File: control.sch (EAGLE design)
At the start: 67 parts, among them IC3 ATTINY85-20S

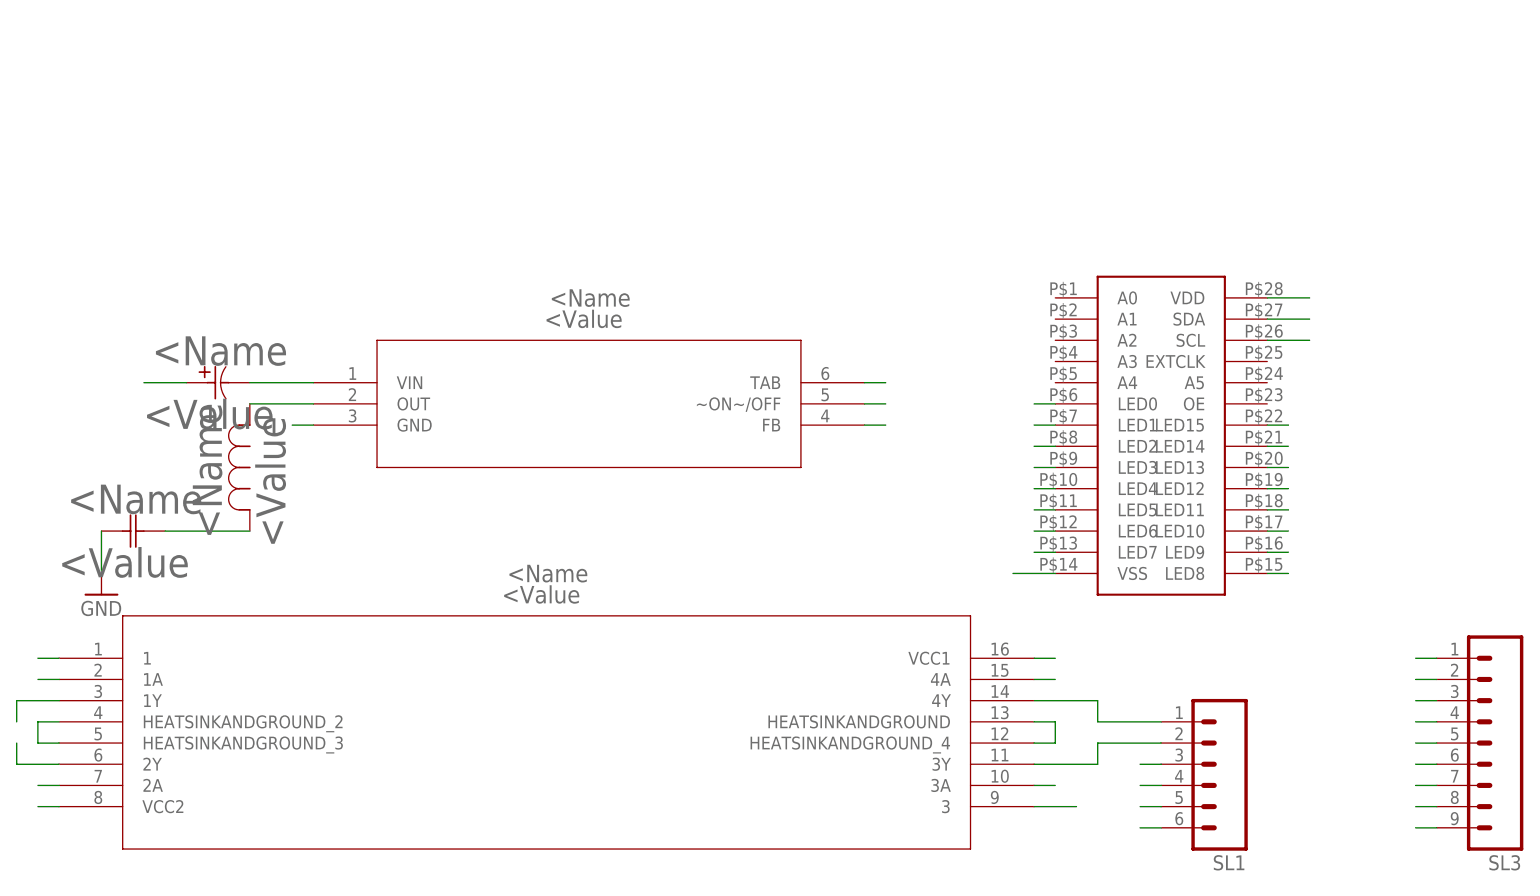
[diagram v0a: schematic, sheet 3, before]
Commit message: adds new components
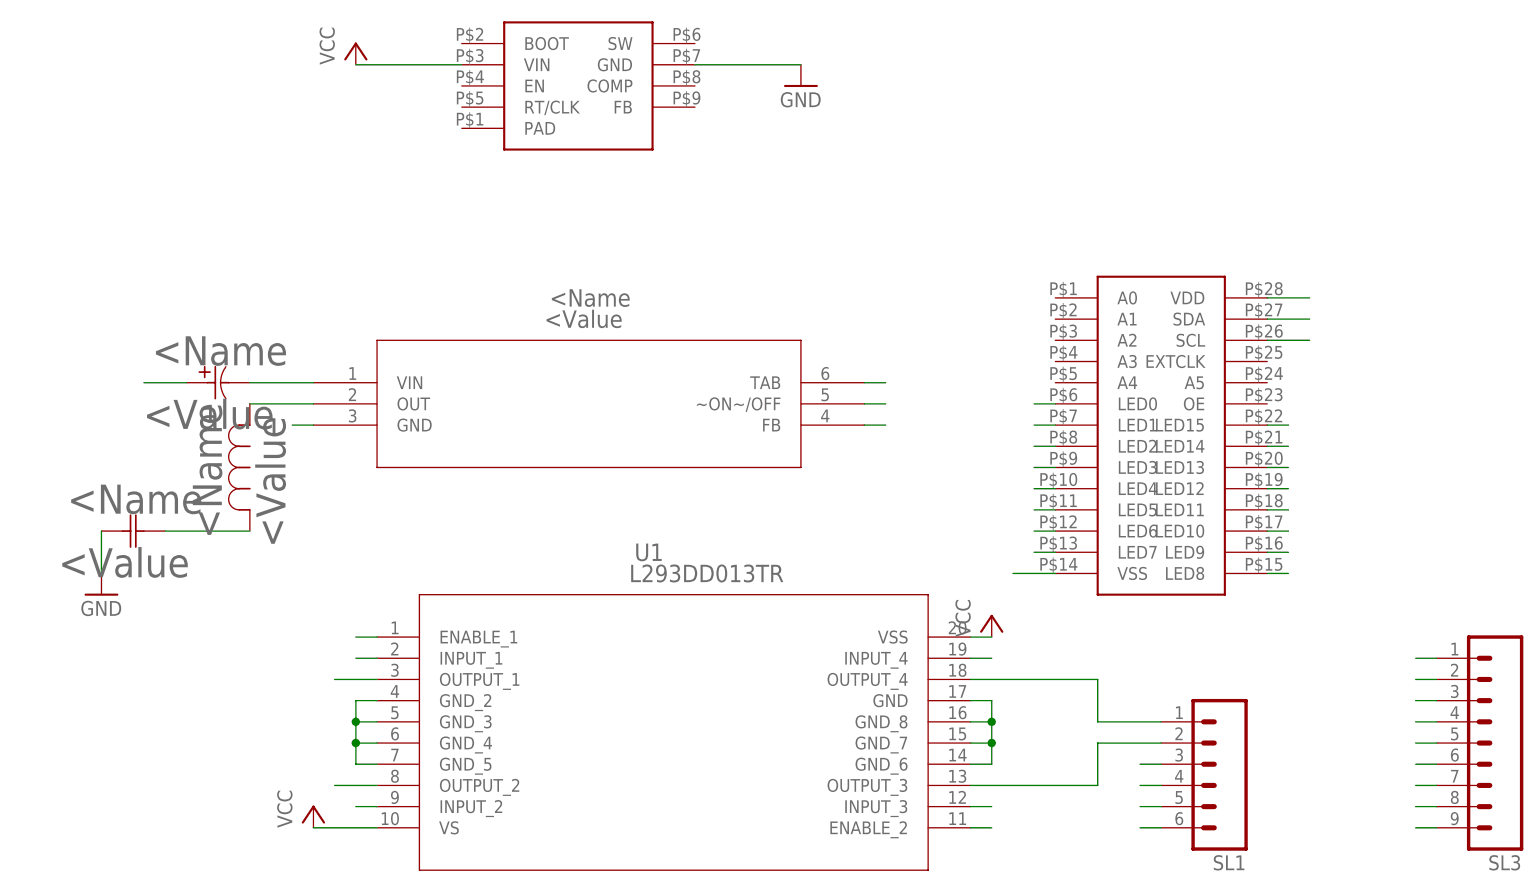
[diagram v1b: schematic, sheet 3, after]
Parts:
- removed U$2: L293DNE, LED Driver:L293DNE
- added U$35: NUD4011DR2G, Smile_Shade:NUD4011DR2G
- added U1: L293DD013TR, Smile_Shade:L293DD013TR
- U$11, U$13, U$15, U$17, U$19, U$21, U$23, U$25, U$27, U$29, U$3, U$31, U$33, U$40, U$5, U$7, U$9: device LED Driver:NUD4011DR2G -> Smile_Shade:NUD4011DR2G
- U$42: value NUD4011DR2G -> TPS54560DDAR; device LED Driver:NUD4011DR2G -> Smile_Shade:TPS54560DDAR
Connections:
- removed net M0: U$1.PWM0, U$2.1
- new net DIR1B: U1.INPUT_2
- new net DIR2A: U1.INPUT_4
- new net DIR2B: U1.INPUT_3
- new net M2: U$1.PWM1, U1.ENABLE_2
- new net N$42: U1.GND_2, U1.GND_3, U1.GND_4, U1.GND_5
- new net N$43: U1.GND, U1.GND_6, U1.GND_7, U1.GND_8
- new net VIN: SL3.1, U$1.CHG-IN, U$42.VIN
- net 3V3: no longer U$2.VCC1
- net 48: now also U$35.VIN; no longer U$40.VIN
- net 48V: now also U$40.VIN; no longer SL3.1, U$42.VIN
- net 5V: now also U1.VSS; no longer U$2.VCC2
- net DIR1A: now also U1.INPUT_1; no longer U$2.2A
- net GND: now also U$42.GND; no longer U$2.HEATSINKANDGROUND, U$2.HEATSINKANDGROUND_2, U$2.HEATSINKANDGROUND_3, U$2.HEATSINKANDGROUND_4
- net LEDSTR_10: now also U$23.LED1, U$23.LED2, U$23.LED3, U$23.LED4; no longer U$21.LED1, U$21.LED2, U$21.LED3, U$21.LED4
- net LEDSTR_11: now also U$21.LED1, U$21.LED2, U$21.LED3, U$21.LED4; no longer U$23.LED1, U$23.LED2, U$23.LED3, U$23.LED4
- net LEDSTR_12: now also U$19.LED1, U$19.LED2, U$19.LED3, U$19.LED4; no longer U$25.LED1, U$25.LED2, U$25.LED3, U$25.LED4
- net LEDSTR_17: now also U$35.LED1, U$35.LED2, U$35.LED3, U$35.LED4; no longer U$40.LED1, U$40.LED2, U$40.LED3, U$40.LED4
- net LEDSTR_18: now also U$40.LED1, U$40.LED2, U$40.LED3, U$40.LED4; no longer U$42.LED1, U$42.LED2, U$42.LED3, U$42.LED4
- net LEDSTR_9: now also U$25.LED1, U$25.LED2, U$25.LED3, U$25.LED4; no longer U$19.LED1, U$19.LED2, U$19.LED3, U$19.LED4
- net M1: now also U$1.PWM0, U1.ENABLE_1; no longer U$1.PWM1, U$2.3
- net M1A: now also U1.OUTPUT_1; no longer U$2.1Y
- net M1B: now also U1.OUTPUT_2; no longer U$2.2Y
- net M2A: now also U1.OUTPUT_4; no longer U$2.4Y
- net M2B: now also U1.OUTPUT_3; no longer U$2.3Y
- net N$17: now also U$25.PWM; no longer U$19.PWM
- net N$18: now also U$25.REXT; no longer U$19.REXT
- net N$19: now also U$23.PWM; no longer U$21.PWM
- net N$20: now also U$23.REXT; no longer U$21.REXT
- net N$21: now also U$21.PWM; no longer U$23.PWM
- net N$22: now also U$21.REXT; no longer U$23.REXT
- net N$23: now also U$19.PWM; no longer U$25.PWM
- net N$24: now also U$19.REXT; no longer U$25.REXT
- net N$35: now also U$35.PWM; no longer U$40.PWM
- net N$36: now also U$35.REXT; no longer U$40.REXT
- net N$37: now also U$40.PWM; no longer U$42.PWM
- net N$38: now also U$40.REXT; no longer U$42.REXT
- net VCC: now also U1.VS; no longer U$1.CHG-IN

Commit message: adds new LED driver
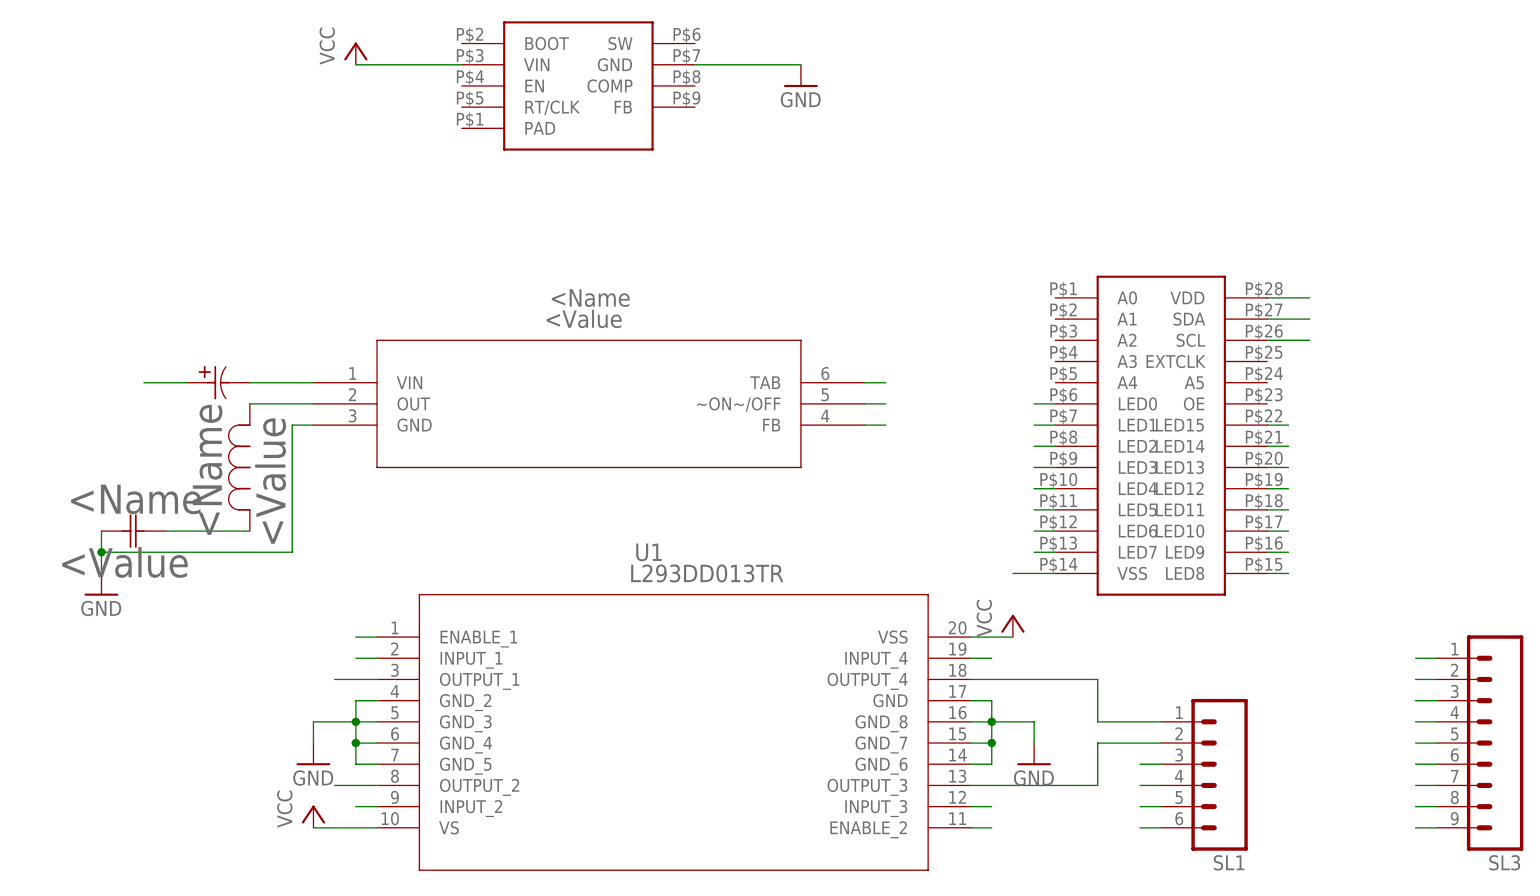
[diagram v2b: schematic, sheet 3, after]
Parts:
- C2: value ESK107M025AE3EA -> UWX1C101MCL1GB; device Smile_Shade:ESK107M025AE3EA -> Smile_Shade:UWX1C101MCL1GB
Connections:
- removed net N$42: U1.GND_2, U1.GND_3, U1.GND_4, U1.GND_5
- removed net N$43: U1.GND, U1.GND_6, U1.GND_7, U1.GND_8
- net DIR1A: now also U$1.CSID4
- net DIR1B: now also U$1.CSID5
- net DIR2A: now also U$1.CSID6
- net DIR2B: now also U$1.CSID7
- net GND: now also U1.GND, U1.GND_2, U1.GND_3, U1.GND_4, U1.GND_5, U1.GND_6, U1.GND_7, U1.GND_8
